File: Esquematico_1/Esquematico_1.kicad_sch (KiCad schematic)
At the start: 1 part, among them U1 4001

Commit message: Testing add a MCU
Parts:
- added U2: STM32F405RGTx, Package_QFP:LQFP-64_10x10mm_P0.5mm, symbol MCU_ST_STM32F4:STM32F405RGTx
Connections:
- new net: U2.18 (VSS), U2.63 (VSS)
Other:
- moved on the sheet: U1A
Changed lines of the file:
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@@
 	(paper "A4")
 	(symbol
+		(lib_id "MCU_ST_STM32F4:STM32F405RGTx")
+		(at 184.15 101.6 0)
+		(unit 1)
+		(exclude_from_sim no)
+		(in_bom yes)
+		(on_board yes)
+		(dnp no)
+		(fields_autoplaced yes)
+		(property "Reference" "U2"
+			(at 188.8333 149.86 0)
+			(effects
+				(font
+					(size 1.27 1.27)
+				)
+				(justify left)
+			)
+		)
+		(property "Value" "STM32F405RGTx"
+			(at 188.8333 152.4 0)
+			(effects
+				(font
+					(size 1.27 1.27)
+				)
+				(justify left)
+			)
+		)
+		(property "Footprint" "Package_QFP:LQFP-64_10x10mm_P0.5mm"
+			(at 166.37 147.32 0)
+			(effects
+				(font
+					(size 1.27 1.27)
+				)
+				(justify right)
+				(hide yes)
+			)
+		)
+		(property "Datasheet" "https://www.st.com/resource/en/datasheet/stm32f405rg.pdf"
+			(at 184.15 101.6 0)
+			(effects
+				(font
+					(size 1.27 1.27)
+				)
+				(hide yes)
+			)
+		)
+		(property "Description" "STMicroelectronics Arm Cortex-M4 MCU, 1024KB flash, 192KB RAM, 168 MHz, 1.8-3.6V, 51 GPIO, LQFP64"
+			(at 184.15 101.6 0)
+			(effects
+				(font
+					(size 1.27 1.27)
+				)
+				(hide yes)
+			)
+		)
+		(pin "58"
+		)
+		(pin "63"
+		)
+		(pin "17"
+		)
+		(pin "42"
+		)
+		(pin "45"
+		)
+		(pin "52"
+		)
+		(pin "61"
+		)
+		(pin "44"
+		)
+		(pin "54"
+		)
+		(pin "39"
+		)
+		(pin "21"
+		)
+		(pin "25"
+		)
+		(pin "51"
+		)
+		(pin "5"
+		)
+		(pin "6"
+		)
+		(pin "33"
+		)
+		(pin "7"
+		)
+		(pin "40"
+		)
+		(pin "24"
+		)
+		(pin "30"
+		)
+		(pin "16"
+		)
+		(pin "20"
+		)
+		(pin "18"
+		)
+		(pin "56"
+		)
+		(pin "50"
+		)
+		(pin "19"
+		)
+		(pin "35"
+		)
+		(pin "32"
+		)
+		(pin "1"
+		)
+		(pin "47"
+		)
+		(pin "36"
+		)
+		(pin "27"
+		)
+		(pin "26"
+		)
+		(pin "31"
+		)
+		(pin "48"
+		)
+		(pin "28"
+		)
+		(pin "55"
+		)
+		(pin "57"
+		)
+		(pin "2"
+		)
+		(pin "59"
+		)
+		(pin "22"
+		)
+		(pin "23"
+		)
+		(pin "43"
+		)
+		(pin "60"
+		)
+		(pin "14"
+		)
+		(pin "4"
+		)
+		(pin "37"
+		)
+		(pin "8"
+		)
+		(pin "46"
+		)
+		(pin "53"
+		)
+		(pin "9"
+		)
+		(pin "11"
+		)
+		(pin "13"
+		)
+		(pin "15"
+		)
+		(pin "10"
+		)
+		(pin "62"
+		)
+		(pin "49"
+		)
+		(pin "3"
+		)
+		(pin "64"
+		)
+		(pin "38"
+		)
+		(pin "34"
+		)
+		(pin "29"
+		)
+		(pin "12"
+		)
+		(pin "41"
+		)
+		(instances
+			(project ""
+				(path "/de2d80c1-c21c-478d-b724-17659b714c38"
+					(reference "U2")
+					(unit 1)
+				)
+			)
+		)
+	)
+	(symbol
 		(lib_id "4xxx:4001")
-		(at 135.89 92.71 0)
+		(at 82.55 80.01 0)
 		(unit 1)
 		(exclude_from_sim no)
@@
 		(fields_autoplaced yes)
 		(property "Reference" "U1"
-			(at 135.89 83.82 0)
+			(at 82.55 71.12 0)
 			(effects
 				(font
@@
 		)
 		(property "Value" "4001"
-			(at 135.89 86.36 0)
+			(at 82.55 73.66 0)
 			(effects
 				(font
@@
 		)
 		(property "Footprint" ""
-			(at 135.89 92.71 0)
+			(at 82.55 80.01 0)
 			(effects
 				(font
@@
 		)
 		(property "Datasheet" "http://www.intersil.com/content/dam/Intersil/documents/cd40/cd4000bms-01bms-02bms-25bms.pdf"
-			(at 135.89 92.71 0)
+			(at 82.55 80.01 0)
 			(effects
 				(font
@@
 		)
 		(property "Description" "Quad Nor 2 inputs"
-			(at 135.89 92.71 0)
-			(effects
-				(font
+			(at 82.55 80.01 0)
+			(effects
+				(font

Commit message: Se agregaron las páginas para el trabajo
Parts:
- removed U1: 4001, symbol 4xxx:4001
- removed U2: STM32F405RGTx, Package_QFP:LQFP-64_10x10mm_P0.5mm, symbol MCU_ST_STM32F4:STM32F405RGTx
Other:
- added sheet MCU (microcontrolador.kicad_sch)
- added sheet PowerMangment (power.kicad_sch)
- added sheet Sensores (sensores_.kicad_sch)

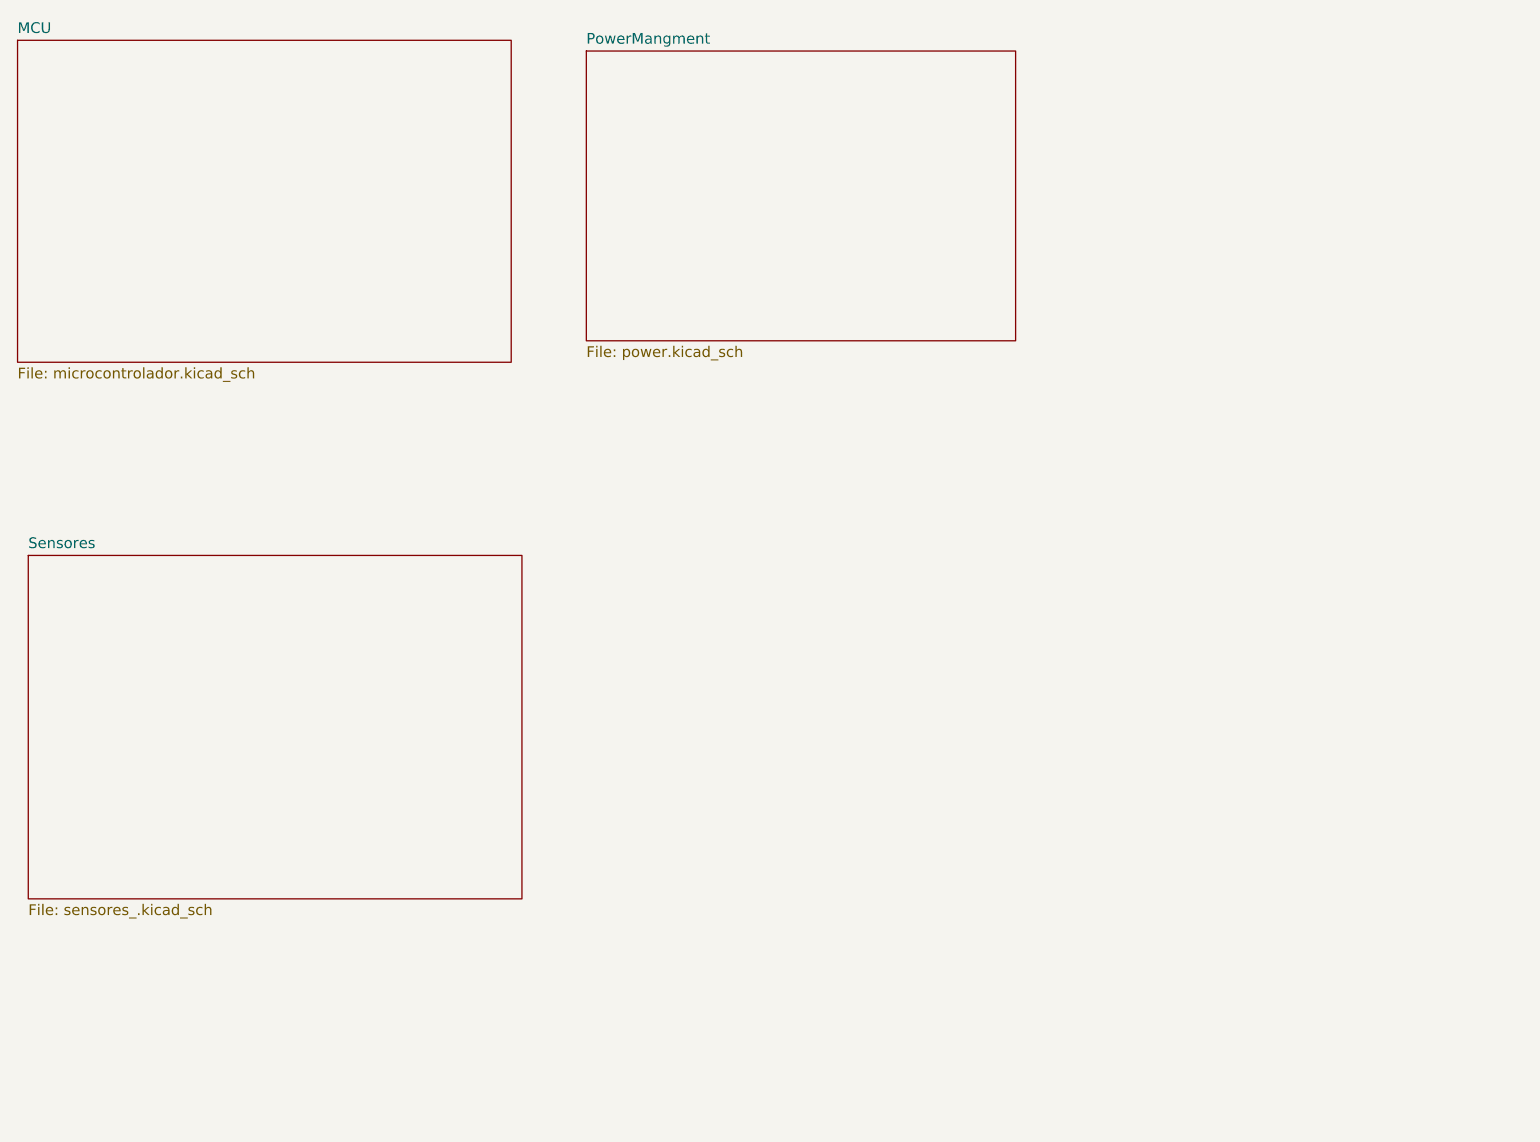
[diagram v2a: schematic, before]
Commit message: OSD added
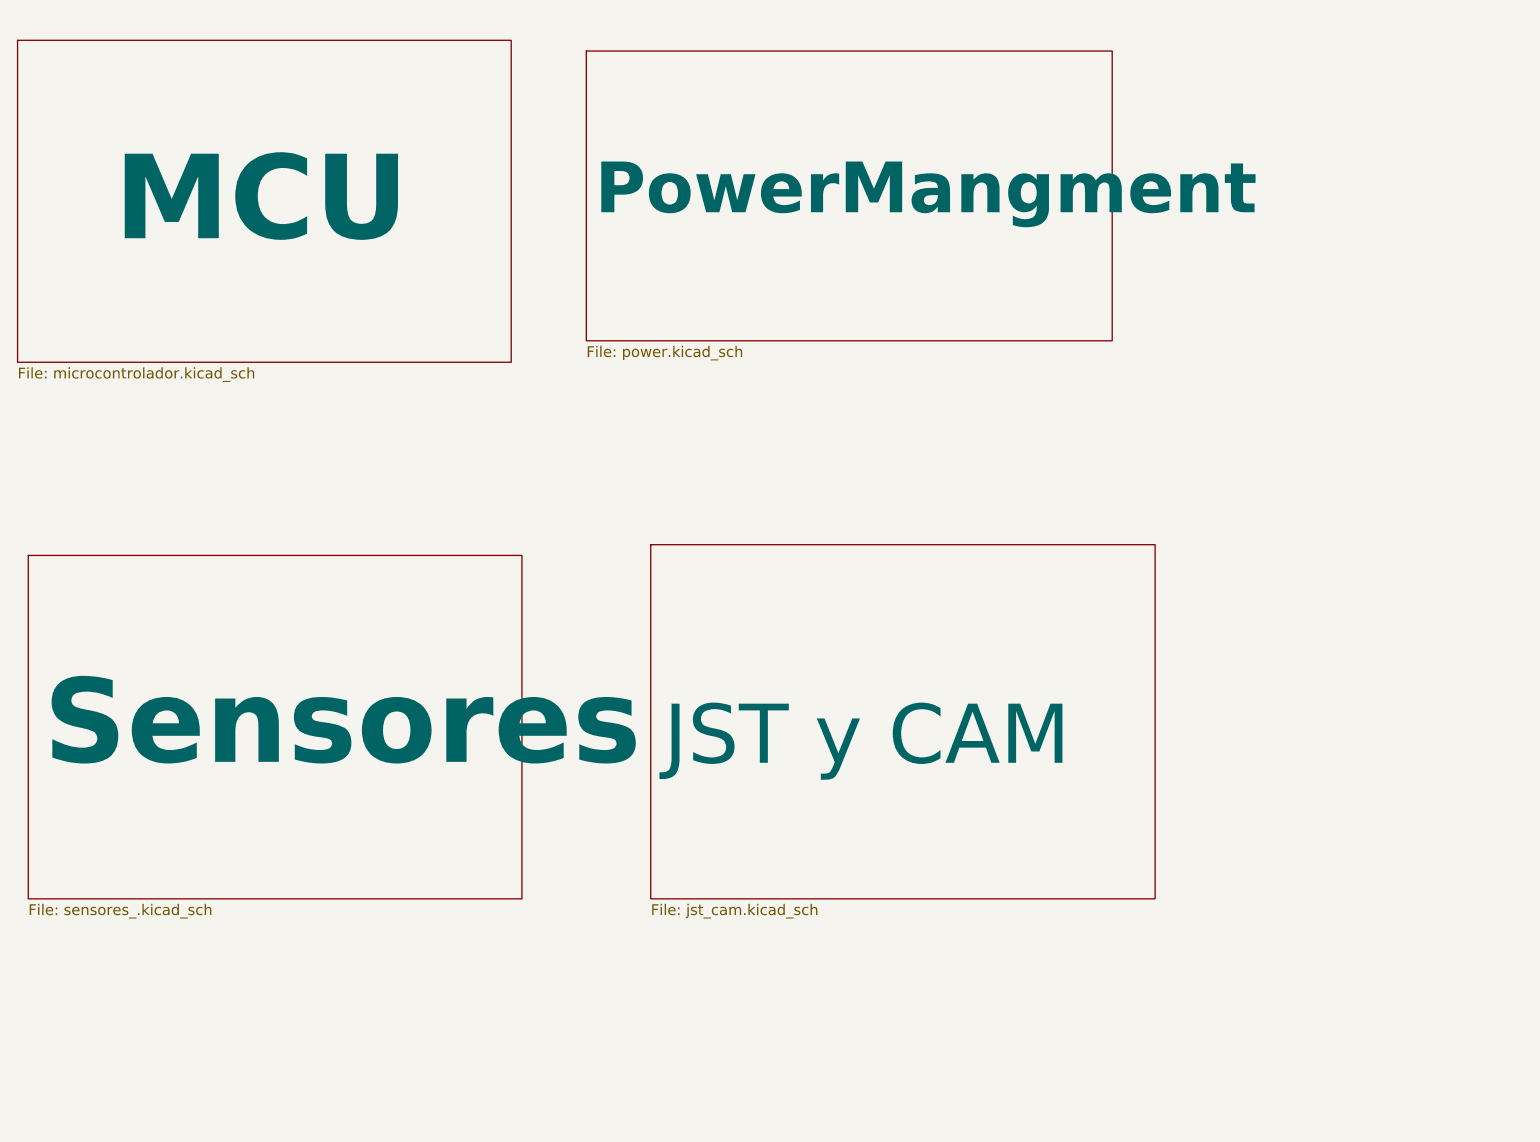
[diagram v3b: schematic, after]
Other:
- added sheet JST y CAM (jst_cam.kicad_sch)
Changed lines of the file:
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@@
 	(paper "A4")
 	(sheet
-		(at 95.25 26.67)
-		(size 50.8 34.29)
+		(at 102.87 85.09)
+		(size 59.69 41.91)
 		(exclude_from_sim no)
 		(in_bom yes)
 		(on_board yes)
 		(dnp no)
-		(fields_autoplaced yes)
+		(stroke
+			(width 0.1524)
+			(type solid)
+		)
+		(fill
+			(color 0 0 0 0.0000)
+		)
+		(property "Sheetname" "JST y CAM"
+			(at 104.394 111.76 0)
+			(effects
+				(font
+					(face "Old English Text MT")
+					(size 7 7)
+				)
+				(justify left bottom)
+			)
+		)
+		(property "Sheetfile" "jst_cam.kicad_sch"
+			(at 102.87 127.5846 0)
+			(effects
+				(font
+					(size 1.27 1.27)
+				)
+				(justify left top)
+			)
+		)
+		(instances
+			(project "Esquematico_1"
+				(path "/de2d80c1-c21c-478d-b724-17659b714c38"
+					(page "5")
+				)
+			)
+		)
+	)
+	(sheet
+		(at 95.25 26.67)
+		(size 62.23 34.29)
+		(exclude_from_sim no)
+		(in_bom yes)
+		(on_board yes)
+		(dnp no)
 		(stroke
 			(width 0.1524)
@@
 		)
 		(property "Sheetname" "PowerMangment"
-			(at 95.25 25.9584 0)
+			(at 96.266 46.482 0)
 			(effects
 				(font
-					(size 1.27 1.27)
+					(face "Old English Text MT")
+					(size 6 6)
+					(thickness 3)
+					(bold yes)
 				)
 				(justify left bottom)
@@
 		(on_board yes)
 		(dnp no)
-		(fields_autoplaced yes)
 		(stroke
 			(width 0.1524)
@@
 		)
 		(property "Sheetname" "Sensores"
-			(at 29.21 85.6484 0)
+			(at 30.988 112.014 0)
 			(effects
 				(font
-					(size 1.27 1.27)
+					(face "Old English Text MT")
+					(size 10 10)
+					(thickness 3)
+					(bold yes)
 				)
 				(justify left bottom)
@@
 		(on_board yes)
 		(dnp no)
-		(fields_autoplaced yes)
 		(stroke
 			(width 0.1524)
@@
 		)
 		(property "Sheetname" "MCU"
-			(at 27.94 24.6884 0)
+			(at 39.37 44.196 0)
 			(effects
 				(font
-					(size 1.27 1.27)
+					(face "Old English Text MT")
+					(size 10 10)
+					(thickness 2)
+					(bold yes)
 				)
-				(justify left bottom)
+				(justify left)
 			)
 		)
